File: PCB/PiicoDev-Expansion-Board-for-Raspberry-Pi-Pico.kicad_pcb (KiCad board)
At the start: 2 copper layers, 50.4 x 51.4 mm, 24 parts, among them J1 PiicoDev, J2 JST PH, J3 , J4 , Q1 Q_PMOS_GSD, U1 MCP73832-2-OT

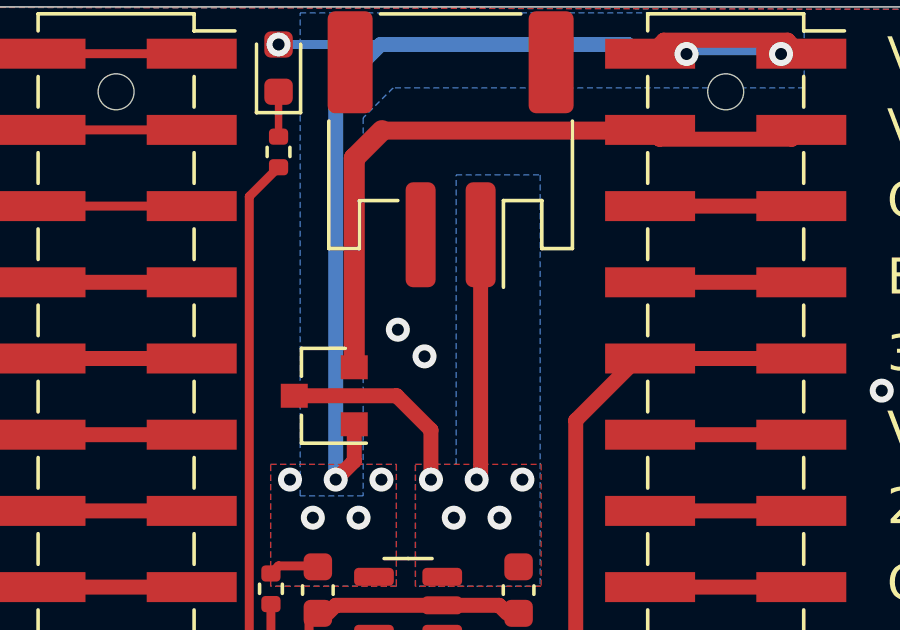
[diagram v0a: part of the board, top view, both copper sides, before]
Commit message: Update links and silk text
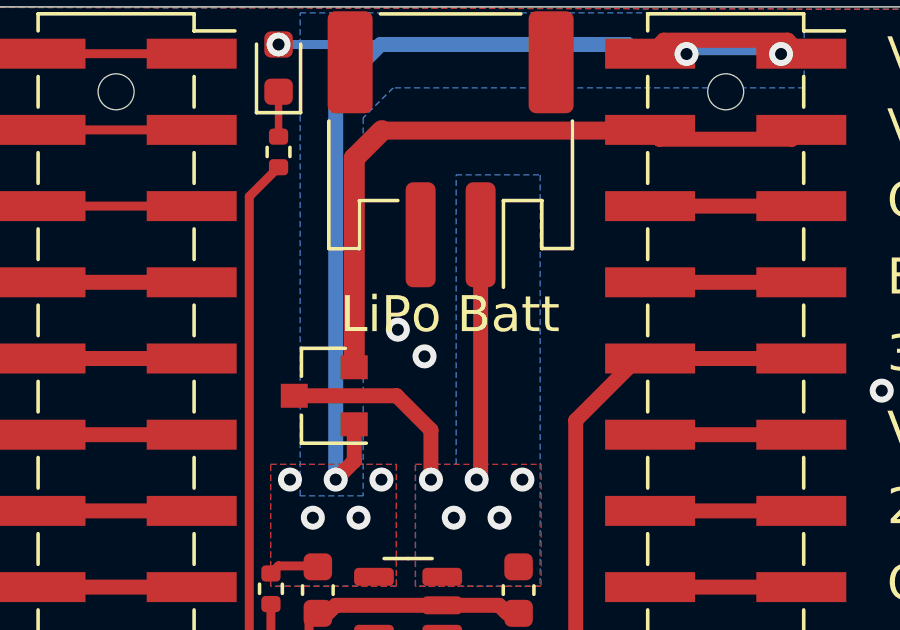
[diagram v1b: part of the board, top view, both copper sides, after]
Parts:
- removed the G*** at (25.4, 32.4)
- added G***: LOGO, CoreElectronics_Artwork:CoreElectronics_logo_5mm, B.Cu at (25.4, 47.6)
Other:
- board text added: "LiPo Batt"
- board text added: "piico.dev/p8"
- board text removed: "coreelec.io/rpico"

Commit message: Add 120R to SCL & SDA. Improve silk screen.
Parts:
- added R7: 120R, Resistor_SMD:R_0402_1005Metric, F.Cu at (20.2, 35.9)
- added R8: 120R, Resistor_SMD:R_0402_1005Metric, F.Cu at (22.8, 35.9)
- Q1: value Q_PMOS_GSD -> DMG3415U-7
- moved R6 2.76 mm to (24.0, 35.9)
- moved R5 1.77 mm to (21.5, 35.9)
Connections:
- J1 pad 3: /I2C0_SDA -> Net-(J1-Pad3)
- J1 pad 4: /I2C0_SCL -> Net-(J1-Pad4)
- R5 pad 2: /I2C0_SDA -> Net-(J1-Pad3)
- R6 pad 2: /I2C0_SCL -> Net-(J1-Pad4)
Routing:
- net /I2C0_SCL: track 32.6 -> 13.7 mm, vias 2 -> 0
- net /I2C0_SDA: track 33.6 -> 16.9 mm
- net Net-(J1-Pad3): track 0.00 -> 16.1 mm
- net Net-(J1-Pad4): track 0.00 -> 16.1 mm
- net Net-(JP2-Pad1): track 8.44 -> 6.52 mm
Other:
- board text added: "v11"
- board text removed: "v10"
